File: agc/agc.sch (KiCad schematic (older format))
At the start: 120 parts, among them J1 SMA_DAC, J2 SMA_LPTR, J3 SMA_DRIVER, J4 SMA_RX, K1 TR, K2 CONN_3, K3 VIN, K4 CONN_3, K5 TR, K6 TR, K7 HVMON, P1 COUPLED_TEST, P2 FWD_FAULT, P3 REF_FAULT, P4 REF_FAULT, P5 COUPLED_TEST, P6 TP_VCC, P7 COUPLED_TEST, P8 COUPLED_TEST, P9 COUPLED_TEST, U1 BA08CC0WFP, U10 74AHC1G04, U12 78SRH-5/2-C, U2 HMC475, U3 HMC595, U4 HMC595, U5 HMC595, U6 74AHC1G04, U7 ISL3281E, U8 MGA-61563, U9 LTC2914-2

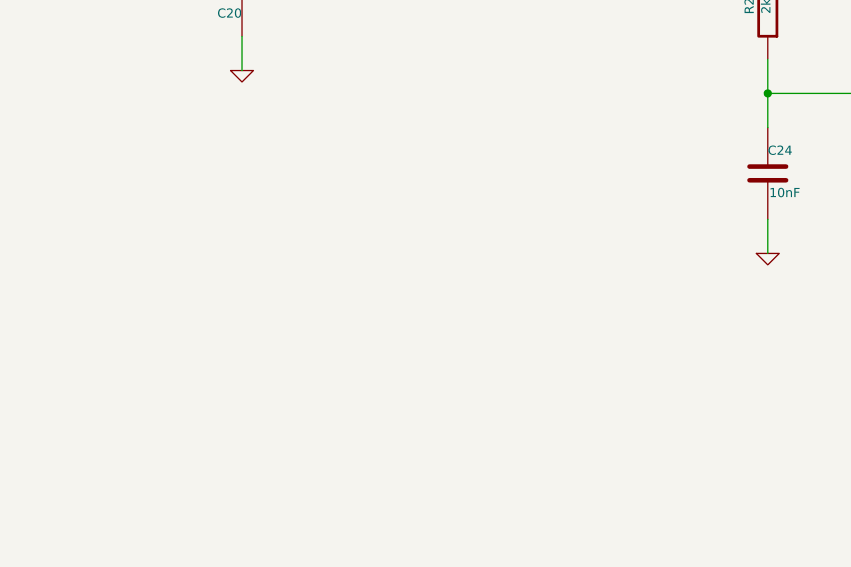
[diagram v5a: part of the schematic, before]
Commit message: work on analog front end board
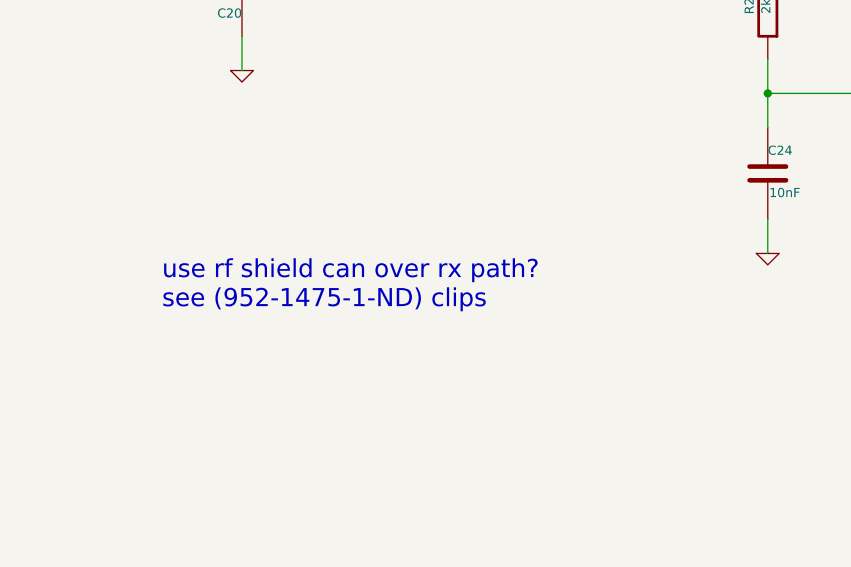
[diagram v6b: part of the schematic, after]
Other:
- note added: "use rf shield can over rx path?\nsee (952-1475-1-ND) clips\n"
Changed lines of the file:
@@
 	8750 12750 10150 12750
 Connection ~ 8050 13000
+Text Notes 9050 4250 0    79   ~ 0
+use rf shield can over rx path?\nsee (952-1475-1-ND) clips\n
 $EndSCHEMATC

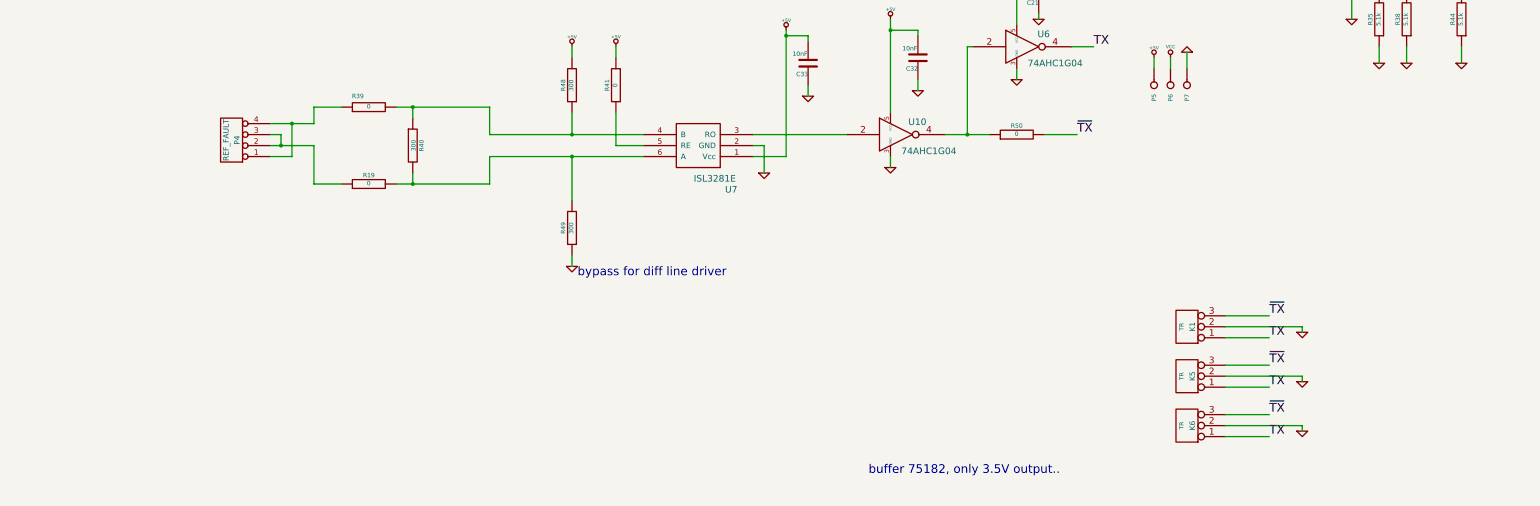
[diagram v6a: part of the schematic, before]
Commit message: layout of usrp header on kodiak control board
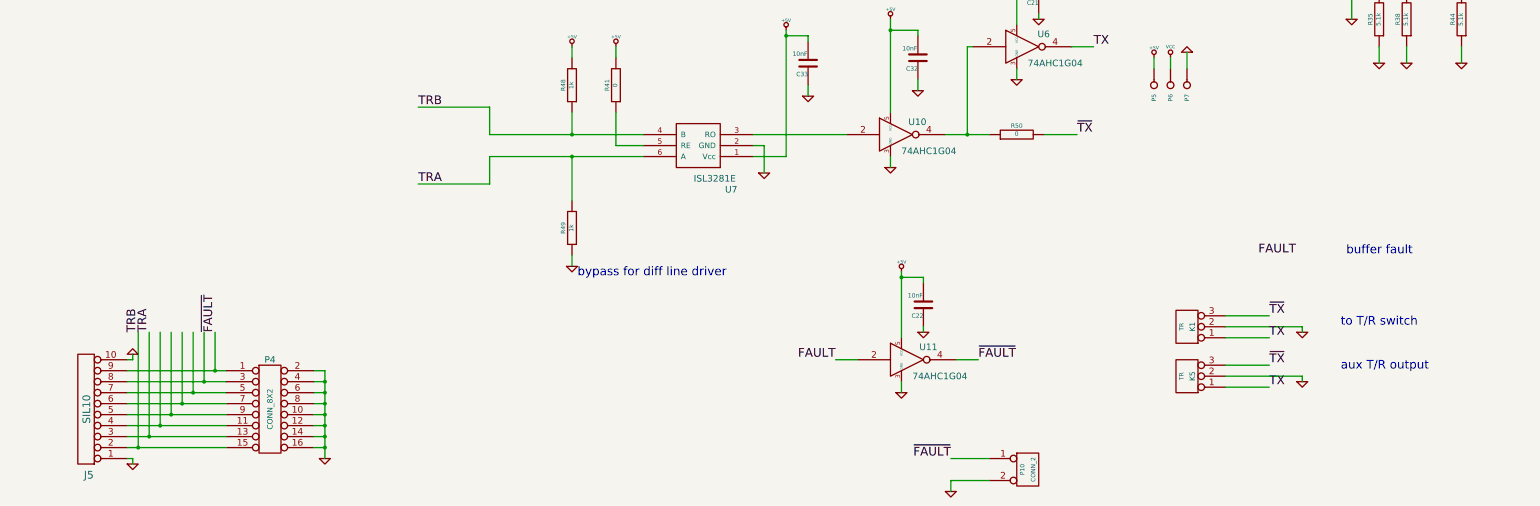
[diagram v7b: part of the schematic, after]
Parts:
- removed K6: TR, Connect:PINHEAD1-3, symbol CONN_3
- removed P4: REF_FAULT, localconn:conn4, symbol CONN_4
- removed R19, R39: 0, SMD_Packages:SM0805, symbol R
- removed R40: 300, SMD_Packages:SM0805, symbol R
- added C22: 10nF, SMD_Packages:SM0805, symbol C
- added J5: SIL10, symbol SIL10
- added P10: CONN_2, symbol CONN_2
- added P4: CONN_8X2, symbol CONN_8X2
- added U11: 74AHC1G04, SMD_Packages:SOT23-5, symbol 74AHC1G04
- R48, R49: value 300 -> 1k
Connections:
- net +5V: now also C22.2, U11.5 (VCC)
- net FAULT: now also U11.2
- net GND: now also C22.1, J5.1, J5.10, P10.2 (PM), P4.10, P4.12, P4.14, P4.16, P4.2, P4.4, P4.6, P4.8, U11.3 (GND)
- net TRA: now reaches R49.2, U7.6 (A)
- net TRA: now also J5.3, P4.13
- net TRB: now reaches R48.1, U7.4 (B)
- net TRB: now also J5.2, P4.15
- new net: J5.4, P4.11
- new net: J5.8, P4.3
- new net: J5.7, P4.5
- new net: J5.6, P4.7
- new net: J5.5, P4.9
- new net ~FAULT: J5.9, P10.1 (P1), P4.1, U11.4
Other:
- note added: "aux T/R output"
- note added: "buffer fault\n"
- note added: "to T/R switch"
- note removed: "buffer 75182, only 3.5V output.."

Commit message: layout on agc r2
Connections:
- net TRA: now also J5.6, P4.7; no longer J5.3, P4.13
- net TRB: now also J5.5, P4.9; no longer J5.2, P4.15
- new net: J5.3, P4.13
- new net: J5.2, P4.15
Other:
- note removed: "buffer fault\n"
- moved on the sheet: P10
